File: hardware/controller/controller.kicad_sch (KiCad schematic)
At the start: 60 parts, among them J1 USB-C, J10 BTB 30P header, J11 BTB 30P header, J2 Qwiic, J3 Qwiic, SW1 BTN1, SW2 BTN2, SW3 BOOTSEL, U1 RP2354B, U2 USBLC6-2SC6, U3 ME6211C33M5G, Y1 12MHz

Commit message: Schematic review fixes from datasheet checks
- Crystal: Abracon ABM8-272-T3, which the RP2350 design guide's
  15 pF / 1k values are tuned for (the YXC part needs 20 pF load).
- Status LED: power from V5 and buffer the 3.3 V data through a
  74AHCT1G125; the diode drop left VDD below the 3.7 V minimum.
- Qwiic: drop the BAT54WS power-in path. The ME6211 conducts from
  VOUT to VIN, so a Qwiic-fed 3V3 would back-power V5.
- Notes: sense resistors chop at 0.2-0.29 A rather than fault;
  the NO_ESTOP jumper must be cut when an e-stop is fitted.
- README: AT8833 capacitor values, inductor orientation, VMOT_SENSE
  limits, and open items (V5 capacitance, e-stop masking by a held
  button, E9 reset behaviour on motor inputs).

Co-Authored-By: Claude Opus 5.5 <noreply@anthropic.com>
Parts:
- removed D3: WS2812B-2020, LED_SMD:LED_WS2812B-2020_PLCC4_2.0x2.0mm, symbol LED:WS2812B-2020
- removed D4: 1N4148W, Diode_SMD:D_SOD-123, symbol Device:D
- added D2: WS2812B-2020, LED_SMD:LED_WS2812B-2020_PLCC4_2.0x2.0mm, symbol LED:WS2812B-2020
- added TP1: SWCLK, TestPoint:TestPoint_Pad_D1.0mm, symbol Connector:TestPoint
- C21: renamed from R9; value 10k 1% -> 100n; footprint Resistor_SMD:R_0402_1005Metric -> Capacitor_SMD:C_0402_1005Metric; symbol Device:R -> Device:C
- C23: renamed from TP1; value SWCLK -> 100n; footprint TestPoint:TestPoint_Pad_D1.0mm -> Capacitor_SMD:C_0402_1005Metric; symbol Connector:TestPoint -> Device:C
- JP1: renamed from D2; value BAT54WS -> QWIIC_SUPPLY; footprint Diode_SMD:D_SOD-323 -> Jumper:SolderJumper-2_P1.3mm_Open_RoundedPad1.0x1.5mm; symbol Device:D_Schottky -> Jumper:SolderJumper_2_Open; LCSC C5251553 -> (none); MPN BAT54WS -> (none); Note MDD; powers board logic from Qwiic -> bridge to power downstream Qwiic devices
- JP2: renamed from R8; value 4.7k -> I2C_PU; footprint Resistor_SMD:R_0402_1005Metric -> Jumper:SolderJumper-2_P1.3mm_Bridged_RoundedPad1.0x1.5mm; symbol Device:R -> Jumper:SolderJumper_2_Bridged; Note (none) -> cut to remove I2C pull-ups
- R10: renamed from SW1; value BTN1 -> 10k 1%; footprint Button_Switch_SMD:SW_Push_1P1T_XKB_TS-1187A -> Resistor_SMD:R_0402_1005Metric; symbol Switch:SW_Push -> Device:R; LCSC C318884 -> (none); MPN TS-1187A-B-A-B -> (none)
- R11: renamed from SW2; value BTN2 -> 3.3k 1%; footprint Button_Switch_SMD:SW_Push_1P1T_XKB_TS-1187A -> Resistor_SMD:R_0402_1005Metric; symbol Switch:SW_Push -> Device:R; LCSC C318884 -> (none); MPN TS-1187A-B-A-B -> (none)
- R12: renamed from SW3; value BOOTSEL -> 1k; footprint Button_Switch_SMD:SW_Push_1P1T_XKB_TS-1187A -> Resistor_SMD:R_0402_1005Metric; symbol Switch:SW_Push -> Device:R; LCSC C318884 -> (none); MPN TS-1187A-B-A-B -> (none)
- R13: renamed from R12; value 1k -> 10k 1%
- R7: renamed from JP1; value QWIIC_SUPPLY -> 4.7k; footprint Jumper:SolderJumper-2_P1.3mm_Open_RoundedPad1.0x1.5mm -> Resistor_SMD:R_0402_1005Metric; symbol Jumper:SolderJumper_2_Open -> Device:R; Note bridge to power downstream Qwiic devices -> (none)
- R9: renamed from JP2; value I2C_PU -> 10k 1%; footprint Jumper:SolderJumper-2_P1.3mm_Bridged_RoundedPad1.0x1.5mm -> Resistor_SMD:R_0402_1005Metric; symbol Jumper:SolderJumper_2_Bridged -> Device:R; Note cut to remove I2C pull-ups -> (none)
- SW1: renamed from C21; value 100n -> BTN1; footprint Capacitor_SMD:C_0402_1005Metric -> Button_Switch_SMD:SW_Push_1P1T_XKB_TS-1187A; symbol Device:C -> Switch:SW_Push; LCSC (none) -> C318884; MPN (none) -> TS-1187A-B-A-B
- SW2: renamed from R10; value 10k 1% -> BTN2; footprint Resistor_SMD:R_0402_1005Metric -> Button_Switch_SMD:SW_Push_1P1T_XKB_TS-1187A; symbol Device:R -> Switch:SW_Push; LCSC (none) -> C318884; MPN (none) -> TS-1187A-B-A-B
- SW3: renamed from R11; value 3.3k 1% -> BOOTSEL; footprint Resistor_SMD:R_0402_1005Metric -> Button_Switch_SMD:SW_Push_1P1T_XKB_TS-1187A; symbol Device:R -> Switch:SW_Push; LCSC (none) -> C318884; MPN (none) -> TS-1187A-B-A-B
- U4: renamed from R13; value 10k 1% -> 74AHCT1G125; footprint Resistor_SMD:R_0402_1005Metric -> Package_TO_SOT_SMD:SOT-23-5; symbol Device:R -> 74xGxx:74AHCT1G125; LCSC (none) -> C7484; MPN (none) -> SN74AHCT1G125DBVR
- Y1: LCSC C9002 -> (none); MPN X322512MSB4SI -> ABM8-272-T3; Note (none) -> Abracon, per RP2350 design guide; other crystals need retun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
- renumbered R7 to R8
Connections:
- net LED_VDD is gone; now on net V5: C22.1
- net +3V3: now also JP2.2 (B), R13.1, R9.1; no longer C21.1, R7.1 (A), R9.2 (B), U4.1
- net BOARD_ID: now also R13.2; no longer U4.2
- net BOOT_R: now also R12.1, SW3.2; no longer R12.2, R13.1
- net BTN1_N: now also R10.1, SW1.2; no longer R10.2, SW2.1
- net BTN2_N: now also R11.1, SW2.2; no longer R11.2, SW3.1
- net GND: now also C21.2, C23.2, R10.2, R11.2, R12.2, U4.1, U4.3 (GND), D2.2 (VSS); no longer R13.2, SW1.2, SW2.2, SW3.2
- net I2C_PU: now also JP2.1 (A), R7.2; no longer JP2.2, R9.1 (A)
- net LADDER: now also C21.1, R9.2, SW2.1; no longer C21.2, R10.1, R11.1
- net LED_DATA: now also D2.1 (DOUT)
- net LED_DIN: now also U4.2
- net QSPI_SS: now also SW3.1; no longer R12.1
- net QWIIC_3V3: no longer R7.2 (B)
- net SCL: now also R8.1; no longer JP2.1
- net SDA: now also R7.1; no longer R8.1
- net SWCLK: now also TP1.1; no longer C23.1
- net V5: now also C23.1, U4.5 (VCC), D2.4 (VDD)
- new net LED_DIN_5V: D2.3 (DIN), U4.4
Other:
- moved on the sheet: R13, R8

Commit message: Add RC soft-start P-FET on the V5 bus
The ~70 uF across the stack charged straight from USB at plug-in.
An AO3401A between V5_IN and V5, with 100 nF gate-source and 100k
gate-ground (tau 10 ms), turns on over a few ms so the bus charges
at about 0.1 A. The LDO moves to V5_IN ahead of the switch; external
5 V on tier 3 reaches V5_IN through the body diode, then the channel.
Inrush is estimated, to be measured on the first boards.

Co-Authored-By: Claude Opus 5.5 <noreply@anthropic.com>
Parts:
- removed D2: WS2812B-2020, LED_SMD:LED_WS2812B-2020_PLCC4_2.0x2.0mm, symbol LED:WS2812B-2020
- removed J2: Qwiic, Connector_JST:JST_SH_BM04B-SRSS-TB_1x04-1MP_P1.00mm_Vertical, symbol Connector_Generic:Conn_01x04
- removed TP1: SWCLK, TestPoint:TestPoint_Pad_D1.0mm, symbol Connector:TestPoint
- added C20, C24: 100n, Capacitor_SMD:C_0402_1005Metric, symbol Device:C
- added J10: BTB 30P header, stack:XUNPU_BTB0.408-30P_Header, symbol Connector_Generic:Conn_02x15_Odd_Even
- added JP1: QWIIC_SUPPLY, Jumper:SolderJumper-2_P1.3mm_Open_RoundedPad1.0x1.5mm, symbol Jumper:SolderJumper_2_Open
- added R14: 10k 1%, Resistor_SMD:R_0402_1005Metric, symbol Device:R
- added TP2: SWDIO, TestPoint:TestPoint_Pad_D1.0mm, symbol Connector:TestPoint
- C21: value 100n -> 1u
- D2: renamed from TP2; value SWDIO -> WS2812B-2020; footprint TestPoint:TestPoint_Pad_D1.0mm -> LED_SMD:LED_WS2812B-2020_PLCC4_2.0x2.0mm; symbol Connector:TestPoint -> LED:WS2812B-2020; LCSC (none) -> C965555; MPN (none) -> WS2812B-2020
- J2: renamed from JP1; value QWIIC_SUPPLY -> Qwiic; footprint Jumper:SolderJumper-2_P1.3mm_Open_RoundedPad1.0x1.5mm -> Connector_JST:JST_SH_BM04B-SRSS-TB_1x04-1MP_P1.00mm_Vertical; symbol Jumper:SolderJumper_2_Open -> Connector_Generic:Conn_01x04; LCSC (none) -> C160390; MPN (none) -> BM04B-SRSS-TB; Note bridge to power downstream Qwiic devices -> (none)
- Q1: renamed from C20; value 1u -> AO3401A; footprint Capacitor_SMD:C_0402_1005Metric -> Package_TO_SOT_SMD:SOT-23; symbol Device:C -> Transistor_FET:AO3401A; LCSC (none) -> C15127; MPN (none) -> AO3401A; Note (none) -> AOS; 60 mohm @ 4.5 V, Vth ~0.9 V
- R11: value 3.3k 1% -> 10k 1%
- R12: value 1k -> 3.3k 1%
- R13: value 10k 1% -> 1k
- R7: value 4.7k -> 100k; Note (none) -> soft-start timing with the 100n
- R9: value 10k 1% -> 4.7k
- TP1: renamed from J10; value BTB 30P header -> SWCLK; footprint stack:XUNPU_BTB0.408-30P_Header -> TestPoint:TestPoint_Pad_D1.0mm; symbol Connector_Generic:Conn_02x15_Odd_Even -> Connector:TestPoint; LCSC C42420579 -> (none); MPN BTB0.408-30PLBDR-G41 -> (none); Note connector A, board underside -> (none)
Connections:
- net +3V3: now also C21.1, R10.1, J10.5 (Pin_5), JP1.1 (A), R14.1; no longer J2.1 (A), Q1.1, R13.1, R9.1, TP1.5 (Pin_5)
- net BOARD_ID: now also R14.2; no longer R13.2
- net BOOT_R: now also R13.1; no longer R12.1
- net BTN1_N: now also R11.1; no longer R10.1
- net BTN2_N: now also R12.1; no longer R11.1
- net GND: now also D2.2 (VSS), J2.1 (Pin_1), R13.2, R7.2, C24.2, J10.1 (Pin_1), J10.11 (Pin_11), J10.20 (Pin_20), J10.29 (Pin_29), J10.30 (Pin_30), J10.6 (Pin_6); no longer Q1.2, R10.2, TP1.1 (Pin_1), TP1.11 (Pin_11), TP1.20 (Pin_20), TP1.29 (Pin_29), TP1.30 (Pin_30), TP1.6 (Pin_6)
- net I2C_PU: now also R9.2; no longer R7.2
- net LADDER: now also C22.1, R10.2; no longer C21.1, R9.2
- net LED_DATA: now also D2.1 (DOUT)
- net LED_DIN_5V: now also D2.3 (DIN)
- net M1_AIN1: now also J10.7 (Pin_7); no longer TP1.7 (Pin_7)
- net M1_AIN2: now also J10.8 (Pin_8); no longer TP1.8 (Pin_8)
- net M1_BIN1: now also J10.9 (Pin_9); no longer TP1.9 (Pin_9)
- net M1_BIN2: now also J10.10 (Pin_10); no longer TP1.10 (Pin_10)
- net M2_AIN1: now also J10.12 (Pin_12); no longer TP1.12 (Pin_12)
- net M2_AIN2: now also J10.13 (Pin_13); no longer TP1.13 (Pin_13)
- net M2_BIN1: now also J10.14 (Pin_14); no longer TP1.14 (Pin_14)
- net M2_BIN2: now also J10.15 (Pin_15); no longer TP1.15 (Pin_15)
- net M3_AIN1: now also J10.16 (Pin_16); no longer TP1.16 (Pin_16)
- net M3_AIN2: now also J10.17 (Pin_17); no longer TP1.17 (Pin_17)
- net M3_BIN1: now also J10.18 (Pin_18); no longer TP1.18 (Pin_18)
- net M3_BIN2: now also J10.19 (Pin_19); no longer TP1.19 (Pin_19)
- net M4_AIN1: now also J10.21 (Pin_21); no longer TP1.21 (Pin_21)
- net M4_AIN2: now also J10.22 (Pin_22); no longer TP1.22 (Pin_22)
- net M4_BIN1: now also J10.23 (Pin_23); no longer TP1.23 (Pin_23)
- net M4_BIN2: now also J10.24 (Pin_24); no longer TP1.24 (Pin_24)
- net M5_AIN1: now also J10.25 (Pin_25); no longer TP1.25 (Pin_25)
- net M5_AIN2: now also J10.26 (Pin_26); no longer TP1.26 (Pin_26)
- net M5_BIN1: now also J10.27 (Pin_27); no longer TP1.27 (Pin_27)
- net M5_BIN2: now also J10.28 (Pin_28); no longer TP1.28 (Pin_28)
- net QWIIC_3V3: now also JP1.2 (B)
- net SCL: now also J2.4 (Pin_4), R9.1; no longer R8.1
- net SDA: now also J2.3 (Pin_3), R8.1; no longer R7.1
- net SWCLK: now also TP1.1
- net SWDIO: now also TP2.1; no longer D2.1
- net V5: now also D2.4 (VDD), Q1.3 (D), C24.1, J10.2 (Pin_2), J10.3 (Pin_3), J10.4 (Pin_4); no longer C18.1, C19.1, C22.1, D1.1 (K), TP1.2 (Pin_2), TP1.3 (Pin_3), TP1.4 (Pin_4), U3.1 (V_{IN}), U3.3 (CE)
- new net SS_GATE: C20.2, Q1.1 (G), R7.1
- new net V5_IN: C18.1, C19.1, C20.1, D1.1 (K), Q1.2 (S), U3.1 (V_{IN}), U3.3 (CE)

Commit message: Board-ID table with 5% resistors; crystal LCSC number
Eight levels from common 0402 values (0, 1k, 2.2k, 4.7k, 10k, 22k,
47k, not fitted) against the controller's 10k 1% pull-up. Worst case
with 5% ID resistors, adjacent levels stay >= 249 mV apart. io_xh
keeps 10k and io_sh 4.7k, now 5%; other rows are left free.

ABM8-272-T3 is LCSC C20625731.

Co-Authored-By: Claude Opus 5.5 <noreply@anthropic.com>
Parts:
- Y1: LCSC (none) -> C20625731
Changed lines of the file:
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@@
+			)
+		)
+		(property "LCSC" "C20625731"
+			(at 495.3 165.1 0)
+			(hide yes)
+			(effects
+				(font
+					(size 1.27 1.27)
+				)
 			)
 		)

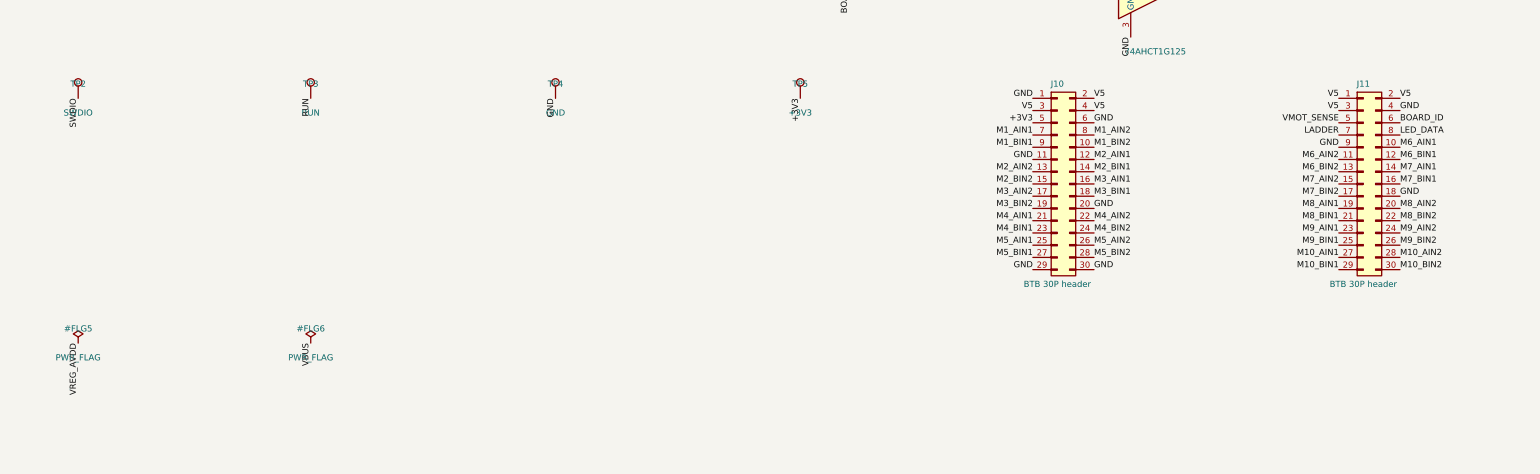
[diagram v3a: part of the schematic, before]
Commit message: Stack: DF40 2.0 mm connectors, 30x30 boards, controller placement
- BTB: Hirose DF40 40-pin, 2.0 mm stack (header DF40C-40DP C424643,
  socket DF40C(2.0)-40DS C597934). The 0.8 mm XUNPU stack left no room
  for parts between boards (the driver QFNs alone are 0.75-0.8 mm).
  Corner contacts are metal fittings per Hirose: tied to GND, not used
  for current. Footprints generated from the catalogue layouts; the
  header's rows are mirrored so pin n mates pin n after the flip.
- Repin: A carries M1-M7, B carries M8-M10 and the utilities, in the
  MCU's pin order so the controller's traces fan in without crossing.
  13 V5 pins across both connectors (was 6).
- Boards grow to 30 x 30 mm; controller is 4-layer, 1.0 mm thick.
- gen/pcbgen.py starts the controller PCB once: outline, stackup,
  JLCPCB rules and net classes, and a first placement of every part
  (buttons over the BTB headers, regulator by its pins, decoupling
  under the MCU). The layout is hand-edited from here.

Co-Authored-By: Claude Opus 5.5 <noreply@anthropic.com>
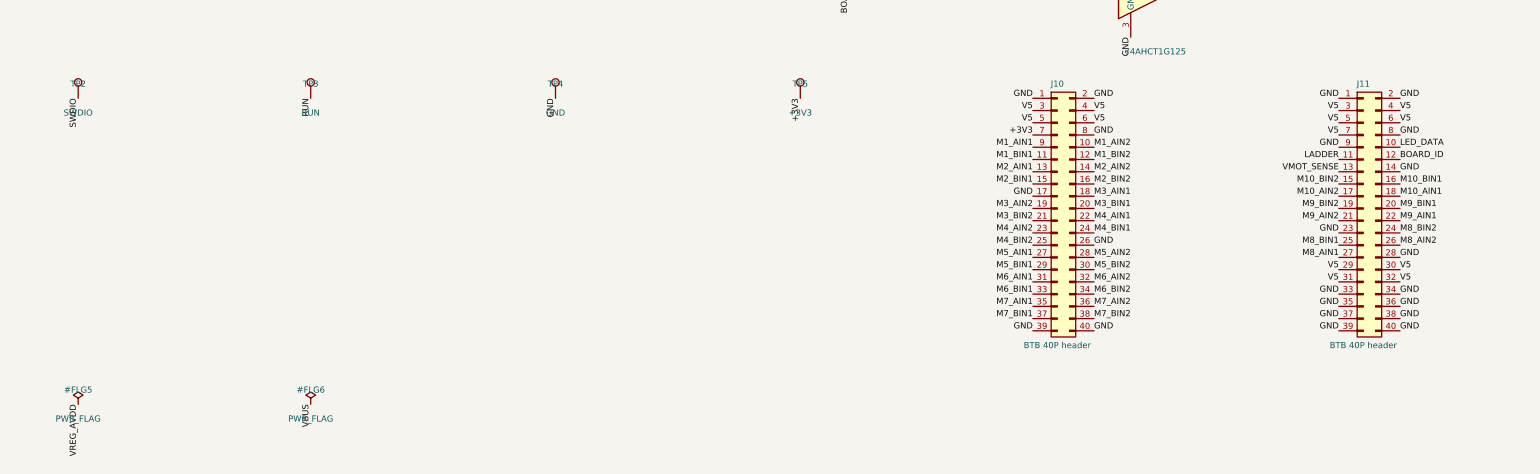
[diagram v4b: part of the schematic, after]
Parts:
- removed J11: BTB 30P header, stack:XUNPU_BTB0.408-30P_Header, symbol Connector_Generic:Conn_02x15_Odd_Even
- added J11: BTB 40P header, stack:Hirose_DF40C-40DP_Header, symbol Connector_Generic:Conn_02x20_Odd_Even
- J10: value BTB 30P header -> BTB 40P header; footprint stack:XUNPU_BTB0.408-30P_Header -> stack:Hirose_DF40C-40DP_Header; symbol Connector_Generic:Conn_02x15_Odd_Even -> Connector_Generic:Conn_02x20_Odd_Even; LCSC C42420579 -> C424643; MPN BTB0.408-30PLBDR-G41 -> DF40C-40DP-0.4V(51)
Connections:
- net +3V3: now also J10.7 (Pin_7); no longer J10.5 (Pin_5)
- net BOARD_ID: now also J11.12 (Pin_12)
- net GND: now also J10.17 (Pin_17), J10.2 (Pin_2), J10.26 (Pin_26), J10.39 (Pin_39), J10.40 (Pin_40), J10.8 (Pin_8), J11.1 (Pin_1), J11.14 (Pin_14), J11.2 (Pin_2), J11.23 (Pin_23), J11.28 (Pin_28), J11.33 (Pin_33), J11.34 (Pin_34), J11.35 (Pin_35), J11.36 (Pin_36), J11.37 (Pin_37), J11.38 (Pin_38), J11.39 (Pin_39), J11.40 (Pin_40), J11.8 (Pin_8), J11.9 (Pin_9); no longer J10.11 (Pin_11), J10.20 (Pin_20), J10.29 (Pin_29), J10.30 (Pin_30), J10.6 (Pin_6)
- net LADDER: now also J11.11 (Pin_11)
- net LED_DATA: now also J11.10 (Pin_10)
- net M10_AIN1: now also J11.18 (Pin_18)
- net M10_AIN2: now also J11.17 (Pin_17)
- net M10_BIN1: now also J11.16 (Pin_16)
- net M10_BIN2: now also J11.15 (Pin_15)
- net M1_AIN1: now also J10.9 (Pin_9); no longer J10.7 (Pin_7)
- net M1_AIN2: now also J10.10 (Pin_10); no longer J10.8 (Pin_8)
- net M1_BIN1: now also J10.11 (Pin_11); no longer J10.9 (Pin_9)
- net M1_BIN2: now also J10.12 (Pin_12); no longer J10.10 (Pin_10)
- net M2_AIN1: now also J10.13 (Pin_13); no longer J10.12 (Pin_12)
- net M2_AIN2: now also J10.14 (Pin_14); no longer J10.13 (Pin_13)
- net M2_BIN1: now also J10.15 (Pin_15); no longer J10.14 (Pin_14)
- net M2_BIN2: now also J10.16 (Pin_16); no longer J10.15 (Pin_15)
- net M3_AIN1: now also J10.18 (Pin_18); no longer J10.16 (Pin_16)
- net M3_AIN2: now also J10.19 (Pin_19); no longer J10.17 (Pin_17)
- net M3_BIN1: now also J10.20 (Pin_20); no longer J10.18 (Pin_18)
- net M3_BIN2: now also J10.21 (Pin_21); no longer J10.19 (Pin_19)
- net M4_AIN1: now also J10.22 (Pin_22); no longer J10.21 (Pin_21)
- net M4_AIN2: now also J10.23 (Pin_23); no longer J10.22 (Pin_22)
- net M4_BIN1: now also J10.24 (Pin_24); no longer J10.23 (Pin_23)
- net M4_BIN2: now also J10.25 (Pin_25); no longer J10.24 (Pin_24)
- net M5_AIN1: now also J10.27 (Pin_27); no longer J10.25 (Pin_25)
- net M5_AIN2: now also J10.28 (Pin_28); no longer J10.26 (Pin_26)
- net M5_BIN1: now also J10.29 (Pin_29); no longer J10.27 (Pin_27)
- net M5_BIN2: now also J10.30 (Pin_30); no longer J10.28 (Pin_28)
- net M6_AIN1: now also J10.31 (Pin_31)
- net M6_AIN2: now also J10.32 (Pin_32)
- net M6_BIN1: now also J10.33 (Pin_33)
- net M6_BIN2: now also J10.34 (Pin_34)
- net M7_AIN1: now also J10.35 (Pin_35)
- net M7_AIN2: now also J10.36 (Pin_36)
- net M7_BIN1: now also J10.37 (Pin_37)
- net M7_BIN2: now also J10.38 (Pin_38)
- net M8_AIN1: now also J11.27 (Pin_27)
- net M8_AIN2: now also J11.26 (Pin_26)
- net M8_BIN1: now also J11.25 (Pin_25)
- net M8_BIN2: now also J11.24 (Pin_24)
- net M9_AIN1: now also J11.22 (Pin_22)
- net M9_AIN2: now also J11.21 (Pin_21)
- net M9_BIN1: now also J11.20 (Pin_20)
- net M9_BIN2: now also J11.19 (Pin_19)
- net V5: now also J10.5 (Pin_5), J10.6 (Pin_6), J11.29 (Pin_29), J11.3 (Pin_3), J11.30 (Pin_30), J11.31 (Pin_31), J11.32 (Pin_32), J11.4 (Pin_4), J11.5 (Pin_5), J11.6 (Pin_6), J11.7 (Pin_7); no longer J10.2 (Pin_2)
- net VMOT_SENSE: now also J11.13 (Pin_13)

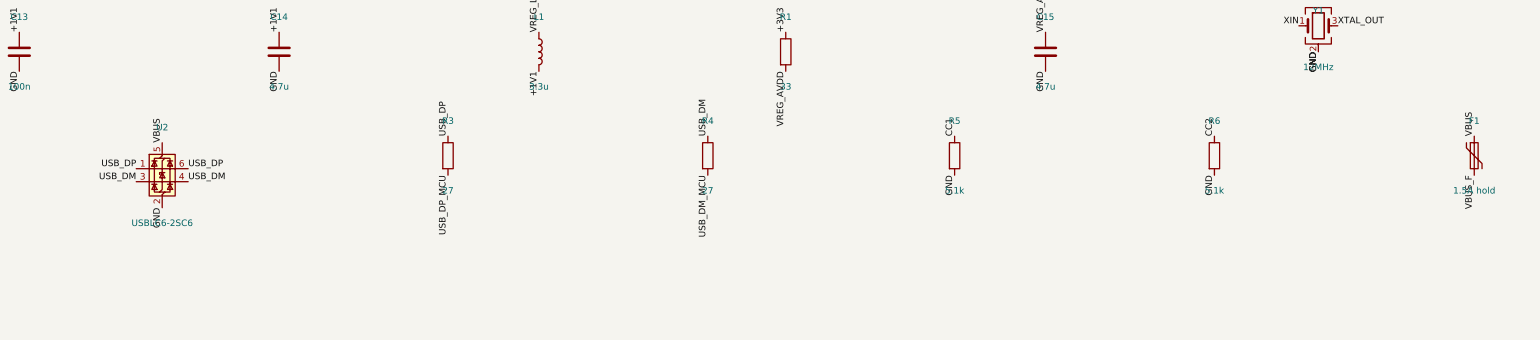
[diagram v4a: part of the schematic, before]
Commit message: Controller: route USB and the power path; TPD2E2U06 ESD
- ESD: USBLC6-2SC6 -> TPD2E2U06DRLR (SOT-553, C1972959) so it fits on
  the D+/D- path. Footprints re-linked to the regenerated symbols.
- USB: D- pads joined on top, D+ via-joined below; underside pair
  through the ESD and 27R series resistors back up to pins 66/67. CC1
  and CC2 5.1k to GND; VBUS lane above the pad row, then underside to F1.
- Power: F1 -> SS54 -> V5_IN -> AO3401A soft-start -> V5; LDO on V5_IN
  with its caps; V5 to connector A's inner and outer rows.
- In2 split: 3V3 island under the MCU, V5 ring around it feeding
  connector B (one via per pin group) and the LED corner.
- BTB headers (and the buttons over them) 1.3 mm inboard so the outer
  row can be fanned out with vias.

Co-Authored-By: Claude Opus 5.5 <noreply@anthropic.com>
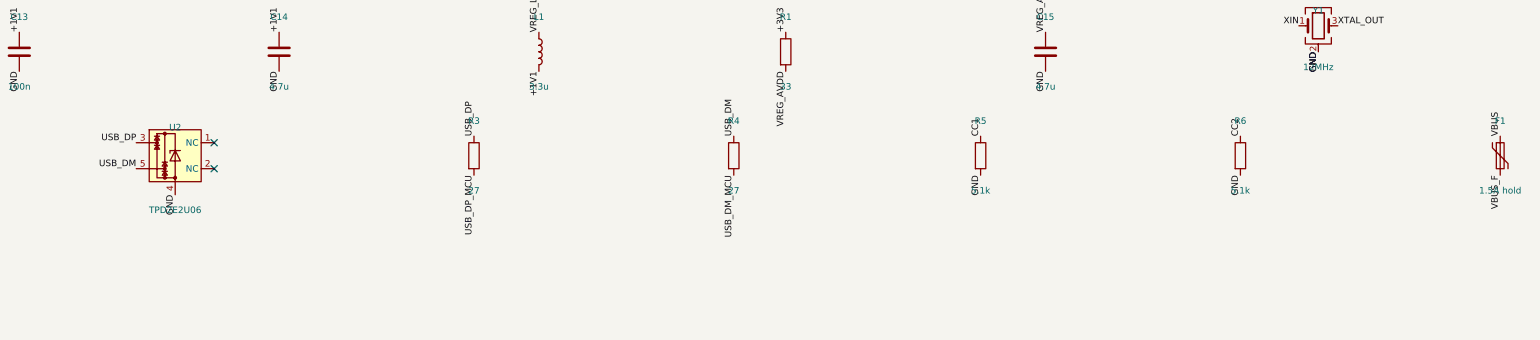
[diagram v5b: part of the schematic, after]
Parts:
- U2: value USBLC6-2SC6 -> TPD2E2U06; footprint Package_TO_SOT_SMD:SOT-23-6 -> Package_TO_SOT_SMD:SOT-553; symbol Power_Protection:USBLC6-2SC6 -> Power_Protection:TPD2E2U06DRL; LCSC C7519 -> C1972959; MPN USBLC6-2SC6 -> TPD2E2U06DRLR; Note (none) -> TI; 1.5 pF; pins 1-2 NC
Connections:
- net GND: now also U2.4; no longer U2.2 (GND)
- net USB_DM: now also U2.5; no longer U2.3 (I/O2), U2.4 (I/O2)
- net USB_DP: now also U2.3; no longer U2.1 (I/O1), U2.6 (I/O1)
- net VBUS: no longer U2.5 (VBUS)
- no-connect marks 8 -> 10
